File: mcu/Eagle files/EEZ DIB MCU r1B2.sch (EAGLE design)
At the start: 189 parts, among them IC1 TPD4E001DRLR, IC10 TPS2051BDBVR, IC11 TPS61169DCKR, IC12 TPD4E001DRLR, IC13 TPA6205A1DGN, IC14 TPD4E001DRLR, IC15 AR1021-I/SS, IC16 TPD4E001DRLR, IC17 DP83848CVV/NOPB, IC2 SN74LVC2G34DBVR, IC3 BTS3408G, IC4 STM32F769IGT6, IC5 LD1117ADT33TR, IC6 TPD4E001DRLR, IC7 TPD4E001DRLR, IC8 IS42S16400J, IC9 BR24G64FVT-3AGE2, J1 503398-1892, J2 67803-8020, Q1 MMBT5551, SW1 PEC16-2215F-S0024, SW2 B3F-3152, X1 ZL263-40DG, X2 ZL231-16KG, X3 1844249, X4 ZL231-20KG, X5 LMJTAB881243M-L, Y1 10MHz

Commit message: SW2 changed
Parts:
- added TP1: (no value), EEZ_Lib1:PCB_TEST_TABSHIELD
- C37: value 10u -> 4u7
- D2: device EEZ_Lib1:SCHOTTKYSOD123 -> EEZ_Lib1:SCHOTTKYSOD-323R
- SW2: value B3F-3152 -> TL1100CF160Q; device EEZ_switches:B3F-315X -> EEZ_switches:TL1100C
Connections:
- net GND: now also TP1.P$1; no longer SW2.GND
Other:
- note added: "Button cap: 4JRED"
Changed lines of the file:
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@@
 <setting verticaltext="up"/>
 </settings>
-<grid distance="0.1" unitdist="inch" unit="inch" style="lines" multiple="1" display="no" altdistance="0.01" altunitdist="inch" altunit="inch"/>
+<grid distance="0.025" unitdist="inch" unit="inch" style="lines" multiple="4" display="no" altdistance="0.01" altunitdist="inch" altunit="inch"/>
 <layers>
 <layer number="1" name="Top" color="4" fill="1" visible="no" active="no"/>
@@
 <part name="SUPPLY51" library="supply2" deviceset="GND" device=""/>
 <part name="SW1" library="EEZ_switches" deviceset="ENCODER_SW" device="-PEC16" value="PEC16-2215F-S0024"/>
-<part name="SW2" library="EEZ_switches" deviceset="B3F-315X" device="" value="B3F-3152"/>
 <part name="SUPPLY116" library="supply2" deviceset="GND" device=""/>
 <part name="SUPPLY92" library="supply2" deviceset="GND" device=""/>
@@
 <part name="R46" library="rcl" deviceset="R-EU_" device="R0805" value="2K2"/>
 <part name="R60" library="rcl" deviceset="R-EU_" device="R0805" value="2K2"/>
-<part name="SUPPLY27" library="supply2" deviceset="GND" device=""/>
 <part name="+3V2" library="supply1" deviceset="+3V3" device=""/>
 <part name="+3V4" library="supply1" deviceset="+3V3" device=""/>
@@
 <part name="+3V34" library="supply1" deviceset="+3V3" device=""/>
 <part name="+3V312" library="supply1" deviceset="+3V3" device=""/>
-<part name="C37" library="rcl" deviceset="C-EU" device="C1206" value="10u"/>
+<part name="C37" library="rcl" deviceset="C-EU" device="C1206" value="4u7"/>
 <part name="SUPPLY26" library="supply2" deviceset="GND" device=""/>
 <part name="SUPPLY18" library="supply2" deviceset="GND" device=""/>
@@
 <part name="+3V317" library="supply1" deviceset="+3V3" device=""/>
 <part name="+3V316" library="supply1" deviceset="+3V3" device=""/>
-<part name="D2" library="EEZ_Lib1" deviceset="SCHOTTKY" device="SOD123" value="RB751V40T1G or NSR0240"/>
+<part name="D2" library="EEZ_Lib1" deviceset="SCHOTTKY" device="SOD-323R" value="RB751V40T1G or NSR0240"/>
 <part name="+3V315" library="supply1" deviceset="+3V3" device=""/>
 <part name="R35" library="rcl" deviceset="R-EU_" device="R0805" value="10K"/>
@@
 <part name="SUPPLY21" library="supply2" deviceset="GND" device=""/>
 <part name="P+9" library="supply1" deviceset="+5V" device=""/>
+<part name="TP1" library="EEZ_Lib1" deviceset="PCB_TEST_TAB" device="SHIELD"/>
+<part name="SW2" library="EEZ_switches" deviceset="TL1100C" device="" value="TL1100CF160Q"/>
 </parts>
 <sheets>
@@
 <text x="5.08" y="175.26" size="1.778" layer="97">Input connector (power, soft start, fan controller)</text>
 <text x="134.62" y="175.26" size="1.778" layer="97">Output connector (3 x SPI modules)</text>
+<text x="229.87" y="53.34" size="1.4224" layer="97">Button cap: 4JRED</text>
 </plain>
 <instances>
@@
 </instance>
 <instance part="SUPPLY51" gate="GND" x="254" y="58.42" smashed="yes">
-<attribute name="VALUE" x="256.54" y="57.15" size="1.778" layer="96"/>
+<attribute name="VALUE" x="252.095" y="59.055" size="1.778" layer="96" rot="R180"/>
 </instance>
 <instance part="SW1" gate="-1" x="172.72" y="68.58" smashed="yes" rot="MR90">
@@
 <attribute name="VALUE" x="167.005" y="79.375" size="1.27" layer="96" rot="R270"/>
 </instance>
-<instance part="SW2" gate="G$1" x="246.38" y="68.58" smashed="yes" rot="R270">
-<attribute name="NAME" x="243.84" y="73.66" size="1.778" layer="95"/>
-<attribute name="VALUE" x="243.205" y="66.04" size="1.778" layer="96" rot="R180"/>
-</instance>
-<instance part="SUPPLY27" gate="GND" x="238.76" y="58.42" smashed="yes">
-<attribute name="VALUE" x="241.3" y="57.15" size="1.778" layer="96"/>
-</instance>
 <instance part="+3V2" gate="G$1" x="213.36" y="129.54" smashed="yes" rot="R270">
 <attribute name="VALUE" x="213.995" y="128.905" size="1.778" layer="96"/>
@@
 <attribute name="VALUE" x="93.98" y="44.45" size="1.778" layer="96"/>
 </instance>
+<instance part="SW2" gate="G$1" x="246.38" y="68.58" smashed="yes">
+<attribute name="NAME" x="243.84" y="72.39" size="1.778" layer="95"/>
+<attribute name="VALUE" x="236.22" y="64.77" size="1.778" layer="96"/>
+</instance>
 </instances>
 <busses>
@@
 <wire x1="238.76" y1="68.58" x2="228.6" y2="68.58" width="0.1524" layer="91"/>
 <label x="228.6" y="69.215" size="1.27" layer="102"/>
-<pinref part="SW2" gate="G$1" pin="1"/>
 <wire x1="238.76" y1="68.58" x2="241.3" y2="68.58" width="0.1524" layer="91"/>
 <junction x="238.76" y="68.58"/>
 <pinref part="C3" gate="G$1" pin="2"/>
+<pinref part="SW2" gate="G$1" pin="1"/>
 </segment>
 </net>
@@
 <wire x1="254" y1="78.74" x2="254" y2="68.58" width="0.1524" layer="91"/>
 <pinref part="SUPPLY51" gate="GND" pin="GND"/>
-<pinref part="SW2" gate="G$1" pin="2"/>
 <wire x1="254" y1="68.58" x2="254" y2="60.96" width="0.1524" layer="91"/>
 <wire x1="251.46" y1="68.58" x2="254" y2="68.58" width="0.1524" layer="91"/>
 <junction x="254" y="68.58"/>
 <pinref part="C3" gate="G$1" pin="1"/>
-</segment>
-<segment>
-<pinref part="SW2" gate="G$1" pin="GND"/>
-<wire x1="241.3" y1="63.5" x2="238.76" y2="63.5" width="0.1524" layer="91"/>
-<wire x1="238.76" y1="63.5" x2="238.76" y2="60.96" width="0.1524" layer="91"/>
-<pinref part="SUPPLY27" gate="GND" pin="GND"/>
+<pinref part="SW2" gate="G$1" pin="2"/>
 </segment>
 <segment>
@@
 <attribute name="VALUE" x="10.795" y="84.455" size="1.778" layer="96" rot="MR180"/>
 </instance>
+<instance part="TP1" gate="G$1" x="241.3" y="60.96" smashed="yes">
+<attribute name="NAME" x="243.205" y="60.325" size="1.778" layer="95"/>
+<attribute name="VALUE" x="241.3" y="58.42" size="1.778" layer="96"/>
+</instance>
 </instances>
 <busses>
@@
 <pinref part="SUPPLY15" gate="GND" pin="GND"/>
 <wire x1="231.14" y1="60.96" x2="231.14" y2="63.5" width="0.1524" layer="91"/>
+<wire x1="231.14" y1="60.96" x2="238.76" y2="60.96" width="0.1524" layer="91"/>
+<junction x="231.14" y="60.96"/>
+<pinref part="TP1" gate="G$1" pin="P$1"/>
 </segment>
 <segment>

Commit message: #12
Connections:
- net !RESET: now also JP4.NO; no longer JP4.NC
- net GND: now also JP4.NC; no longer JP4.NO
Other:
- moved on the sheet: JP4
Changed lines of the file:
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@@
 <setting verticaltext="up"/>
 </settings>
-<grid distance="0.025" unitdist="inch" unit="inch" style="lines" multiple="4" display="no" altdistance="0.01" altunitdist="inch" altunit="inch"/>
+<grid distance="0.1" unitdist="inch" unit="inch" style="lines" multiple="1" display="no" altdistance="0.01" altunitdist="inch" altunit="inch"/>
 <layers>
 <layer number="1" name="Top" color="4" fill="1" visible="no" active="no"/>
@@
 <text x="134.62" y="175.26" size="1.778" layer="97">Output connector (3 x SPI modules)</text>
 <text x="229.87" y="53.34" size="1.4224" layer="97">Button cap: 4JRED</text>
+<wire x1="259.715" y1="175.26" x2="222.885" y2="114.3" width="1.27" layer="100"/>
+<wire x1="220.98" y1="174.625" x2="259.08" y2="116.205" width="1.27" layer="100"/>
+<wire x1="167.64" y1="173.99" x2="186.055" y2="116.205" width="1.27" layer="100"/>
+<wire x1="187.96" y1="174.625" x2="165.1" y2="114.935" width="1.27" layer="100"/>
 </plain>
 <instances>
@@
 <attribute name="VALUE" x="91.567" y="162.941" size="1.778" layer="96"/>
 </instance>
-<instance part="JP4" gate="G$1" x="73.66" y="129.54" smashed="yes">
-<attribute name="NAME" x="73.025" y="128.905" size="1.778" layer="95" rot="MR0"/>
+<instance part="JP4" gate="G$1" x="73.66" y="129.54" smashed="yes" rot="MR180">
+<attribute name="NAME" x="73.025" y="130.175" size="1.778" layer="95" rot="R180"/>
 </instance>
 <instance part="IC13" gate="A" x="223.52" y="66.04" smashed="yes">
@@
 <wire x1="81.28" y1="134.62" x2="86.36" y2="134.62" width="0.1524" layer="91"/>
 <wire x1="81.28" y1="134.62" x2="73.66" y2="134.62" width="0.1524" layer="91"/>
-<wire x1="73.66" y1="134.62" x2="73.66" y2="132.08" width="0.1524" layer="91"/>
 <junction x="81.28" y="134.62"/>
 <pinref part="SUPPLY34" gate="GND" pin="GND"/>
-<pinref part="JP4" gate="G$1" pin="NO"/>
+<pinref part="JP4" gate="G$1" pin="NC"/>
+<wire x1="73.66" y1="132.08" x2="73.66" y2="134.62" width="0.1524" layer="91"/>
 </segment>
 <segment>
@@
 <label x="66.04" y="125.095" size="1.27" layer="102"/>
 <wire x1="73.66" y1="124.46" x2="60.96" y2="124.46" width="0.1524" layer="91"/>
-<wire x1="73.66" y1="124.46" x2="73.66" y2="127" width="0.1524" layer="91"/>
-<pinref part="JP4" gate="G$1" pin="NC"/>
+<pinref part="JP4" gate="G$1" pin="NO"/>
+<wire x1="73.66" y1="127" x2="73.66" y2="124.46" width="0.1524" layer="91"/>
 </segment>
 </net>

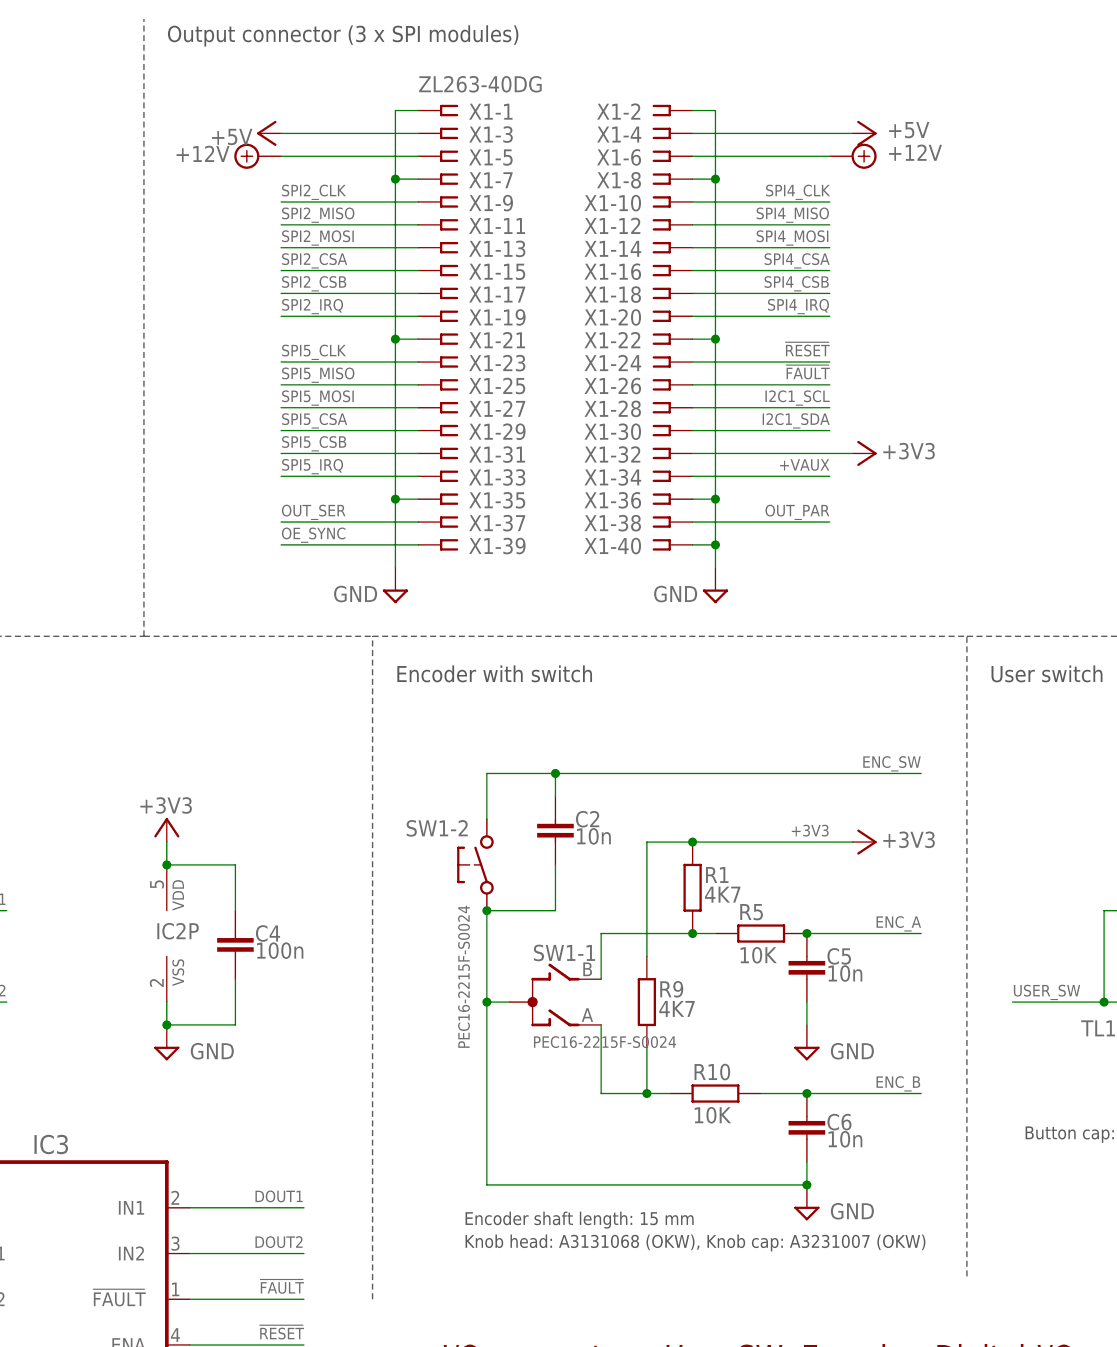
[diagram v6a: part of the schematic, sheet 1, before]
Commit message: MCU fixes: #10, #13, #15, #16, #17, #18
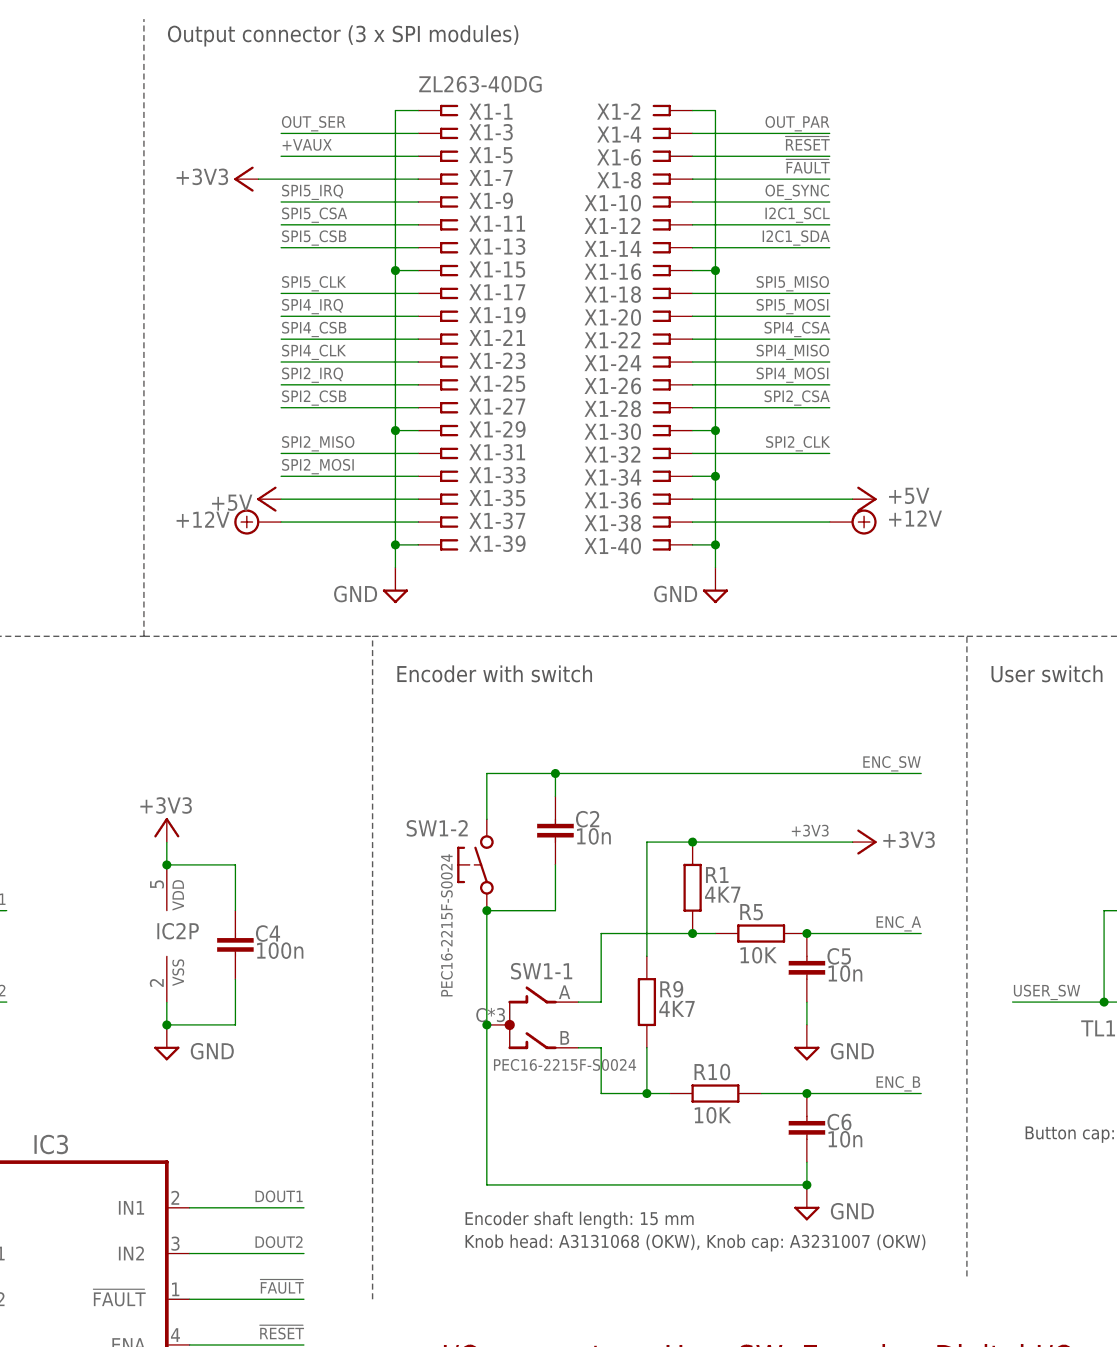
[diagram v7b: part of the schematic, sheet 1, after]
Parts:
- B1: value DS1092-16-B6P -> S8401-46 or DS1092-16-B6P; device EEZ_Lib1:CELL_BATTERY-THT20MM -> EEZ_Lib1:CELL_BATTERYVERT
- IC9: value BR24G64FVT-3AGE2 -> AT24C02D-SSHM-T; device EEZ_DIB:BR24GXXX-TSSOP -> EEZ_Lib1:AT24CXXSOIC8
- R29: value 47K -> 220R
- R59: device rcl:R-EU_R0603 -> rcl:R-EU_R0805
- Y1: value 10MHz -> 25MHz
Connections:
- net !FAULT: now also X1-8.1; no longer X1-26.1
- net !RESET: now also X1-6.1; no longer X1-24.1
- net +12V: now also X1-37.1, X1-38.1; no longer X1-5.1, X1-6.1
- net +3V3: now also VBUS.A, X1-7.1; no longer IC9.A0, IC9.A1, IC9.A2, IC9.WP, X1-32.1
- net +5V: now also X1-35.1, X1-36.1; no longer VBUS.A, X1-3.1, X1-4.1
- net +VAUX: now also X1-5.1; no longer X1-34.1
- net EOUT_A: now also SW1-1.B; no longer SW1-1.A
- net EOUT_B: now also SW1-1.A; no longer SW1-1.B
- net GND: now also IC9.A0, IC9.A1, IC9.A2, IC9.WP, X1-15.1, X1-16.1, X1-29.1, X1-30.1, X1-34.1, X1-39.1; no longer X1-21.1, X1-22.1, X1-35.1, X1-36.1, X1-7.1, X1-8.1
- net I2C1_SCL: now also IC9.SCL, X1-12.1; no longer IC9.SDA, X1-28.1
- net I2C1_SDA: now also IC9.SDA, X1-14.1; no longer IC9.SCL, X1-30.1
- net N$166: now also SP1.-; no longer SP1.+
- net N$50: now also SP1.+; no longer SP1.-
- net OE_SYNC: now also X1-10.1; no longer X1-39.1
- net OUT_PAR: now also X1-4.1; no longer X1-38.1
- net OUT_SER: now also X1-3.1; no longer X1-37.1
- net SPI2_CLK: now also X1-32.1; no longer X1-9.1
- net SPI2_CSA: now also X1-28.1; no longer X1-15.1
- net SPI2_CSB: now also X1-27.1; no longer X1-17.1
- net SPI2_IRQ: now also X1-25.1; no longer X1-19.1
- net SPI2_MISO: now also X1-31.1; no longer X1-11.1
- net SPI2_MOSI: now also X1-33.1; no longer X1-13.1
- net SPI4_CLK: now also X1-23.1; no longer X1-10.1
- net SPI4_CSA: now also X1-22.1; no longer X1-16.1
- net SPI4_CSB: now also X1-21.1; no longer X1-18.1
- net SPI4_IRQ: now also X1-19.1; no longer X1-20.1
- net SPI4_MISO: now also X1-24.1; no longer X1-12.1
- net SPI4_MOSI: now also X1-26.1; no longer X1-14.1
- net SPI5_CLK: now also X1-17.1; no longer X1-23.1
- net SPI5_CSA: now also X1-11.1; no longer X1-29.1
- net SPI5_CSB: now also X1-13.1; no longer X1-31.1
- net SPI5_IRQ: now also X1-9.1; no longer X1-33.1
- net SPI5_MISO: now also X1-18.1; no longer X1-25.1
- net SPI5_MOSI: now also X1-20.1; no longer X1-27.1
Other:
- note added: "+12V 37"
- note added: "+3V3 7"
- note added: "+5V 35"
- note added: "+Vaux 5"
- note added: "10 OE_SYNC"
- note added: "12 I2C_SCL"
- note added: "14 I2C_SDA"
- note added: "16 Gnd"
- note added: "18 CH3_MISO"
- note added: "20 CH3_MOSI"
- note added: "22 CH2_CSA"
- note added: "24 CH2_MISO"
- note added: "26 CH2_MOSI"
- note added: "28 CH1_CSA"
- note added: "30 Gnd"
- note added: "32 CH1_SCLK"
- note added: "34 Gnd"
- note added: "36 +5V"
- note added: "38 +12V"
- note added: "4 OUT_PAR"
- note added: "40-pin MCU socket"
- note added: "6 NRESET"
- note added: "8 NFAULT"
- note added: "CH1_CSB 27"
- note added: "CH1_IRQ 25"
- note added: "CH1_MISO 31"
- note added: "CH1_MOSI 33"
- note added: "CH2_CSB 21"
- note added: "CH2_IRQ 19"
- note added: "CH2_SCLK 23"
- note added: "CH3_CSA 11"
- note added: "CH3_CSB 13"
- note added: "CH3_IRQ 9"
- note added: "CH3_SCLK 17"
- note added: "Gnd 15"
- note added: "Gnd 29"
- note added: "Gnd 3"
- note added: "Gnd 39"
- note added: "NRST 5"
- note added: "OUT_SER 3"
- note added: "STM-32 board SWD header"
- note added: "SWCLK 2"
- note added: "SWDIO 4"
- note added: "SWO 6"
- note added: "Vdd target 1"
- note removed: "+12V 5"
- note removed: "+5V 3"
- note removed: "10 CH2_SCLK"
- note removed: "12 CH2_MISO"
- note removed: "14 CH2_MOSI"
- note removed: "16 CH2_CSA"
- note removed: "18 CH2_CSB"
- note removed: "20 CH2_IRQ"
- note removed: "22 Gnd"
- note removed: "24 NRESET"
- note removed: "26 NFAULT"
- note removed: "28 SSCL"
- note removed: "30 SSDA"
- note removed: "32 +3V3"
- note removed: "34 +VAUX"
- note removed: "36 Gnd"
- note removed: "38 OUT_PAR"
- note removed: "4 +5V"
- note removed: "40-pin bus socket"
- note removed: "6 +12V"
- note removed: "CH1_CSA 15"
- note removed: "CH1_CSB 17"
- note removed: "CH1_IRQ 19"
- note removed: "CH1_MISO 11"
- note removed: "CH1_MOSI 13"
- note removed: "CH1_SCLK 9"
- note removed: "CH3_CSA 29"
- note removed: "CH3_CSB 31"
- note removed: "CH3_IRQ 33"
- note removed: "CH3_MISO 25"
- note removed: "CH3_MOSI 27"
- note removed: "CH3_SCLK 23"
- note removed: "Gnd 21"
- note removed: "Gnd 35"
- note removed: "OE_SYNC 39"
- note removed: "OUT_SER 37"
- note removed: "Skratiti za BR24G08FVJ-3AGTE2 !!!"
- moved on the sheet: B1, R40, SP1, X1-11, X1-13, X1-15, X1-17, X1-19, X1-21, X1-23, X1-25, X1-27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
